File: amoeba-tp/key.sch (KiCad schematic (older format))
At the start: 4 parts

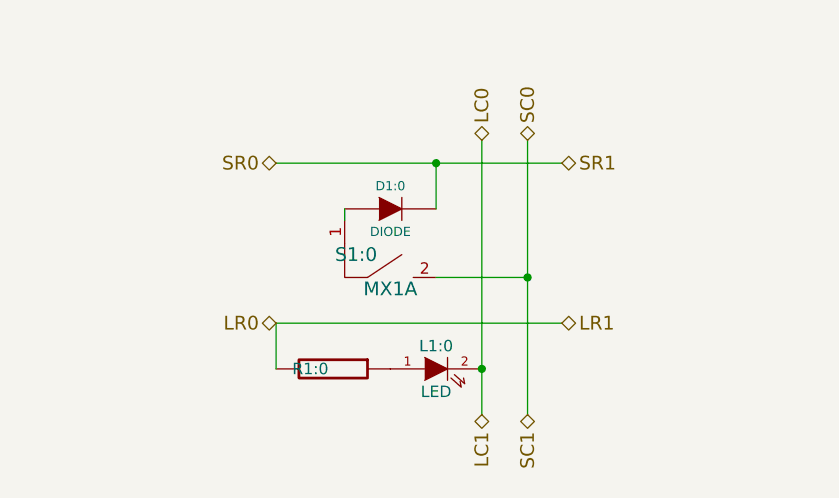
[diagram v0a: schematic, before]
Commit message: Adding SMD options to TP module.
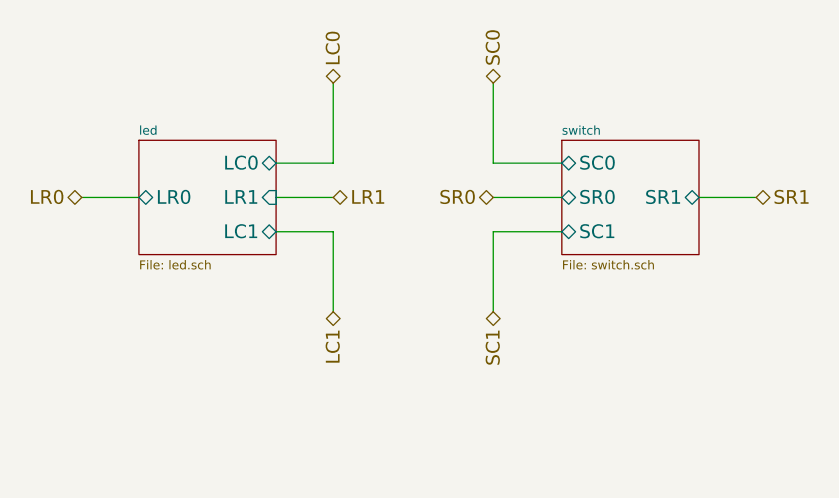
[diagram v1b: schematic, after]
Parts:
- removed D0:0: DIODE, ~, symbol DIODE
- removed L0:0: LED, ~, symbol LED
- removed R0:0: RESISTOR, ~, symbol RESISTOR
- removed S0:0: MX1A, ~, symbol MX1A
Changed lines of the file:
@@
 $Descr A4 11693 8268
 encoding utf-8
-Sheet 3 6
+Sheet 14 16
 Title ""
-Date "24 aug 2015"
+Date "25 aug 2015"
 Rev ""
 Comp ""
@@
 Comment4 ""
 $EndDescr
-$Comp
-L MX1A S0:0
-U 1 1 55D93046
-P 5650 3950
-AR Path="/55D95A82/55D93046" Ref="S0:0"  Part="1"
-AR Path="/55D94306/55D93046" Ref="S0:1"  Part="1"
-AR Path="/55D936FC/55D93046" Ref="S1:0"  Part="1"
-AR Path="/55D94310/55D93046" Ref="S1:1"  Part="1"
-AR Path="/55D9491A/55D93046" Ref="S2:1"  Part="1"
-F 0 "S1:0" H 5500 4200 60  0000 C CNN
-F 1 "MX1A" H 5650 4050 60  0000 C CNN
-F 2 "~" H 5650 3950 60  0000 C CNN
-F 3 "~" H 5650 3950 60  0000 C CNN
-	1    5650 3950
-	1    0    0    -1
-$EndComp
-$Comp
-L DIODE D0:0
-U 1 1 55D9304C
-P 5650 3500
-AR Path="/55D95A82/55D9304C" Ref="D0:0"  Part="1"
-AR Path="/55D94306/55D9304C" Ref="D0:1"  Part="1"
-AR Path="/55D936FC/55D9304C" Ref="D1:0"  Part="1"
-AR Path="/55D94310/55D9304C" Ref="D1:1"  Part="1"
-AR Path="/55D9491A/55D9304C" Ref="D2:1"  Part="1"
-F 0 "D1:0" H 5650 3600 40  0000 C CNN
-F 1 "DIODE" H 5650 3400 40  0000 C CNN
-F 2 "~" H 5650 3500 60  0000 C CNN
-F 3 "~" H 5650 3500 60  0000 C CNN
-	1    5650 3500
-	1    0    0    -1
-$EndComp
-$Comp
-L LED L0:0
-U 1 1 55D93052
-P 5850 4200
-AR Path="/55D95A82/55D93052" Ref="L0:0"  Part="1"
-AR Path="/55D94306/55D93052" Ref="L0:1"  Part="1"
-AR Path="/55D936FC/55D93052" Ref="L1:0"  Part="1"
-AR Path="/55D94310/55D93052" Ref="L1:1"  Part="1"
-AR Path="/55D9491A/55D93052" Ref="L2:1"  Part="1"
-F 0 "L1:0" H 5850 4300 50  0000 C CNN
-F 1 "LED" H 5850 4100 50  0000 C CNN
-F 2 "~" H 5850 4200 60  0000 C CNN
-F 3 "~" H 5850 4200 60  0000 C CNN
-	1    5850 4200
-	1    0    0    -1
-$EndComp
-$Comp
-L RESISTOR R0:0
-U 1 1 55D93058
-P 5400 4200
-AR Path="/55D95A82/55D93058" Ref="R0:0"  Part="1"
-AR Path="/55D94306/55D93058" Ref="R0:1"  Part="1"
-AR Path="/55D936FC/55D93058" Ref="R1:0"  Part="1"
-AR Path="/55D94310/55D93058" Ref="R1:1"  Part="1"
-AR Path="/55D9491A/55D93058" Ref="R2:1"  Part="1"
-F 0 "R1:0" V 5400 4100 50  0000 C CNN
-F 1 "RESISTOR" H 5400 4300 50  0001 C CNN
-F 2 "~" H 5400 4200 60  0000 C CNN
-F 3 "~" H 5400 4200 60  0000 C CNN
-	1    5400 4200
-	0    1    1    0
-$EndComp
+Text HLabel 5400 2950 1    60   BiDi ~ 0
+LC0
+Text HLabel 5400 3450 2    60   BiDi ~ 0
+LR1
+Text HLabel 4300 3450 0    60   BiDi ~ 0
+LR0
+Text HLabel 5400 3950 3    60   BiDi ~ 0
+LC1
+$Sheet
+S 4550 3200 600  500
+U 55DBAE59
+F0 "led" 39
+F1 "led.sch" 39
+F2 "LC0" B R 5150 3300 60
+F3 "LR0" B L 4550 3450 60
+F4 "LC1" B R 5150 3600 60
+F5 "LR1" I R 5150 3450 60
+$EndSheet
+$Sheet
+S 6400 3200 600  500
+U 55DBAE5B
+F0 "switch" 39
+F1 "switch.sch" 39
+F2 "SC0" B L 6400 3300 60
+F3 "SR1" B R 7000 3450 60
+F4 "SR0" B L 6400 3450 60
+F5 "SC1" B L 6400 3600 60
+$EndSheet
 Wire Wire Line
-	5150 4200 5150 4000
-Connection ~ 6050 4200
+	4550 3450 4300 3450
+Text HLabel 6100 2950 1    60   BiDi ~ 0
+SC0
+Text HLabel 6100 3950 3    60   BiDi ~ 0
+SC1
+Text HLabel 7250 3450 2    60   BiDi ~ 0
+SR1
+Text HLabel 6100 3450 0    60   BiDi ~ 0
+SR0
 Wire Wire Line
-	5850 3800 6250 3800
-Connection ~ 6250 3800
-Connection ~ 5850 3300
+	6400 3450 6100 3450
 Wire Wire Line
-	6050 4400 6050 3200
+	5150 3300 5400 3300
 Wire Wire Line
-	6250 3200 6250 4400
+	5400 3300 5400 2950
 Wire Wire Line
-	5150 3300 6400 3300
+	5150 3450 5400 3450
 Wire Wire Line
-	5150 4000 6400 4000
+	5150 3600 5400 3600
 Wire Wire Line
-	5450 3500 5450 3550
+	5400 3600 5400 3950
 Wire Wire Line
-	5850 3500 5850 3300
-Text HLabel 6250 3200 1    60   BiDi ~ 0
-SC0
-Text HLabel 6050 3200 1    60   BiDi ~ 0
-LC0
-Text HLabel 6400 3300 2    60   BiDi ~ 0
-SR1
-Text HLabel 5150 3300 0    60   BiDi ~ 0
-SR0
-Text HLabel 6400 4000 2    60   BiDi ~ 0
-LR1
-Text HLabel 5150 4000 0    60   BiDi ~ 0
-LR0
-Text HLabel 6050 4400 3    60   BiDi ~ 0
-LC1
-Text HLabel 6250 4400 3    60   BiDi ~ 0
-SC1
+	7250 3450 7000 3450
+Wire Wire Line
+	6400 3300 6100 3300
+Wire Wire Line
+	6100 3300 6100 2950
+Wire Wire Line
+	6100 3950 6100 3600
+Wire Wire Line
+	6100 3600 6400 3600
 $EndSCHEMATC
